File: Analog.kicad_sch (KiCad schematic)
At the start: 17 parts, among them J6 Conn_01x04, U6 MCP602

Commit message: updated pics
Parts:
- C28, C33: value 100n -> 1n
- R11, R12: value 33R -> 160R
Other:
- note added: "LowPass Filt. Fg = 1MHz"
- note removed: "LowPass Filt. Fg = 48.2kHz"
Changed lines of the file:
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@@
-    (effects (font (size 1.27 1.27)) (justify left bottom))
-  )
-  (text "LowPass Filt. Fg = 48.2kHz" (at 167.64 82.55 90)
     (effects (font (size 1.27 1.27)) (justify left bottom))
   )
@@
     (effects (font (size 1.27 1.27)) (justify left bottom))
   )
-  (text "LowPass Filt. Fg = 48.2kHz" (at 52.07 80.01 90)
+  (text "LowPass Filt. Fg = 1MHz" (at 52.07 80.01 90)
     (effects (font (size 1.27 1.27)) (justify left bottom))
   )
@@
   )
   (text "DC filter" (at 213.36 107.95 90)
+    (effects (font (size 1.27 1.27)) (justify left bottom))
+  )
+  (text "LowPass Filt. Fg = 1MHz" (at 166.37 81.28 90)
     (effects (font (size 1.27 1.27)) (justify left bottom))
   )
@@
       (effects (font (size 1.27 1.27)))
     )
-    (property "Value" "33R" (at 165.1 90.17 90)
+    (property "Value" "160R" (at 165.1 90.17 90)
       (effects (font (size 1.27 1.27)))
     )
@@
       (effects (font (size 1.27 1.27)))
     )
-    (property "Value" "100n" (at 172.72 92.71 0)
+    (property "Value" "1n" (at 172.72 92.71 0)
       (effects (font (size 1.27 1.27)))
     )
@@
       (effects (font (size 1.27 1.27)))
     )
-    (property "Value" "100n" (at 58.42 90.17 0)
+    (property "Value" "1n" (at 58.42 90.17 0)
       (effects (font (size 1.27 1.27)))
     )
@@
       (effects (font (size 1.27 1.27)))
     )
-    (property "Value" "33R" (at 50.8 87.63 90)
-      (effects (font (size 1.27 1.27)))
-    )
+    (property "Value" "160R" (at 50.8 87.63 90)
+      (effects (font (size 1.27 1.27)))
+    )

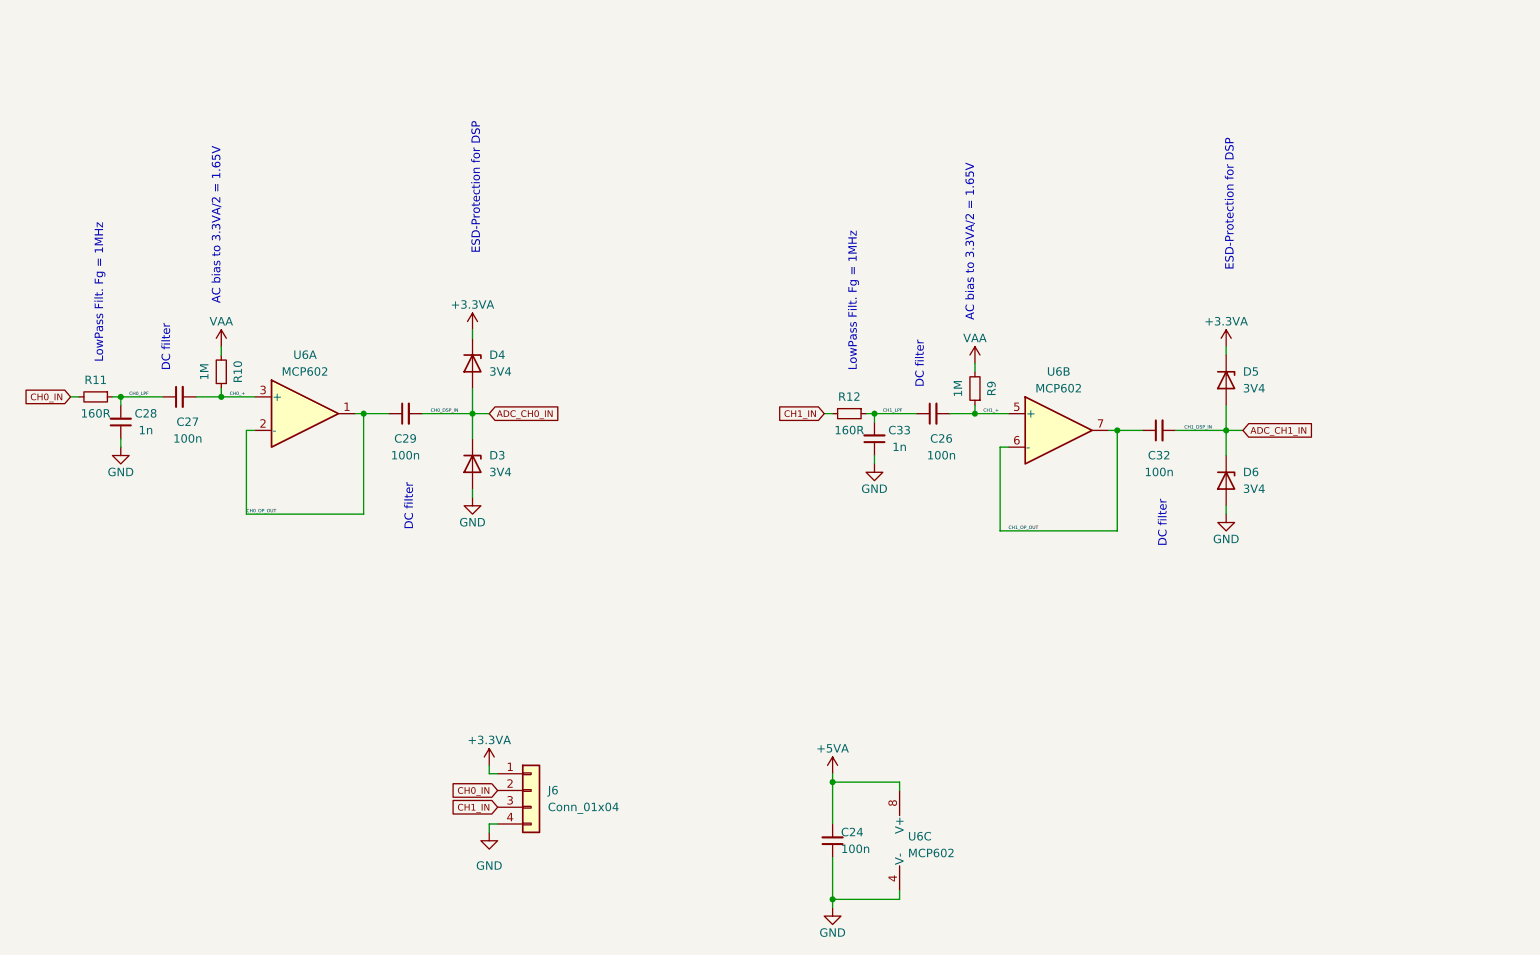
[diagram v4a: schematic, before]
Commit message: added DAC and an onboard fixed oscilltor to quickly test the DSP
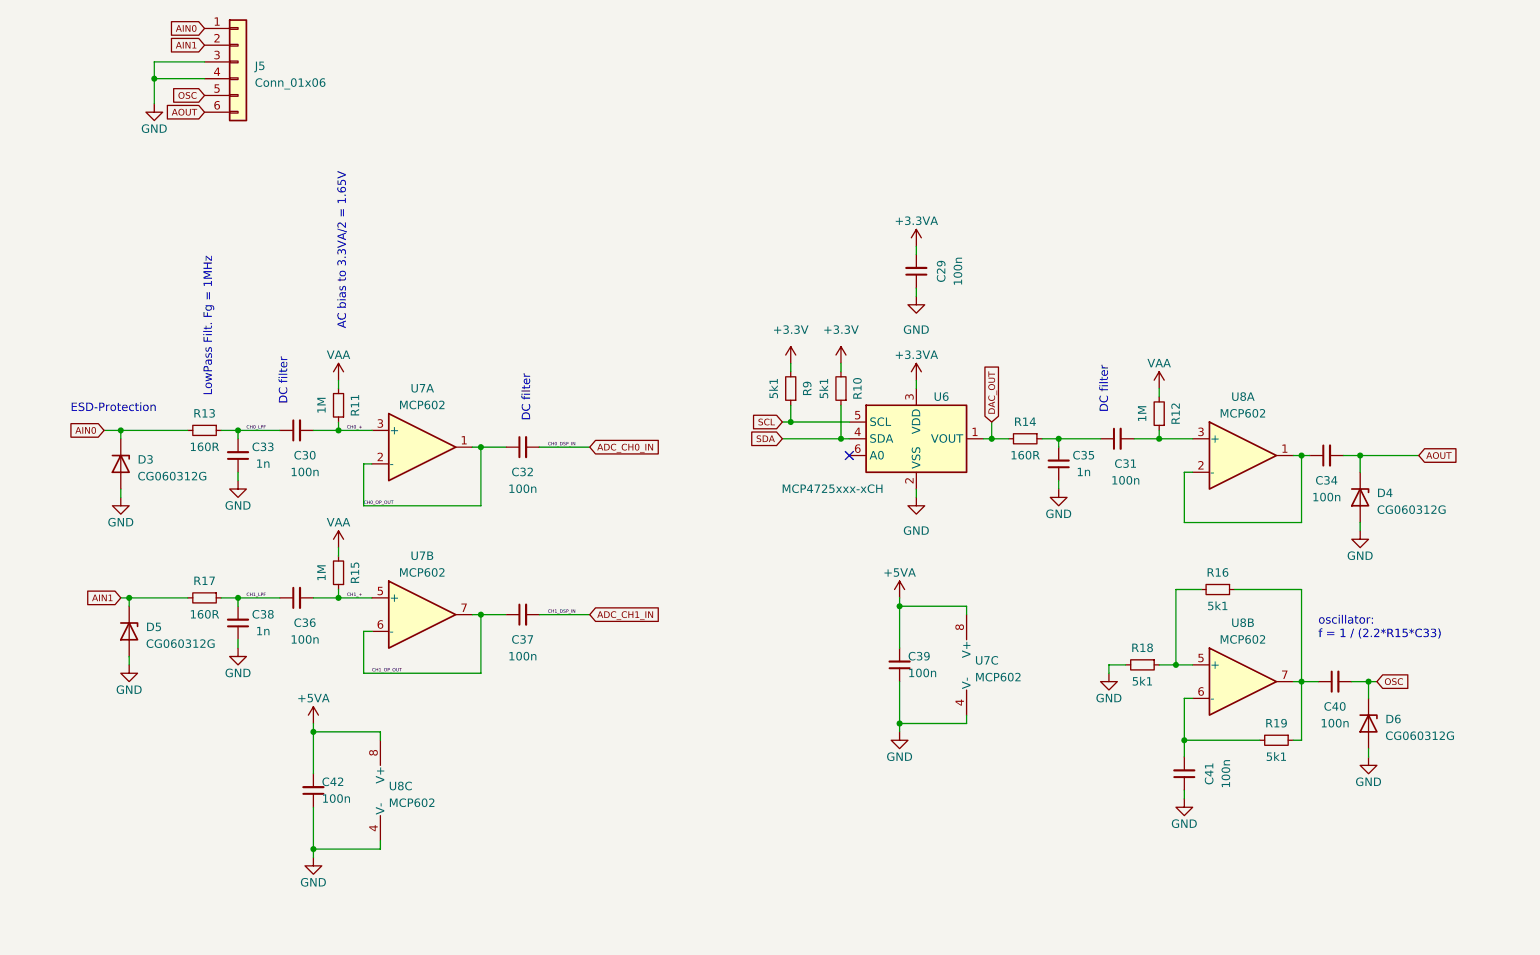
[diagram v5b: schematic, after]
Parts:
- removed D3, D4, D5, D6: 3V4, Diode_SMD:D_SOD-123F, symbol Device:D_Zener
- removed J6: Conn_01x04, Connector_PinHeader_2.54mm:PinHeader_1x04_P2.54mm_Vertical, symbol Connector_Generic:Conn_01x04
- added C29, C31, C34, C39, C40, C41: 100n, Capacitor_SMD:C_0603_1608Metric_Pad1.08x0.95mm_HandSolder, symbol Device:C_Small
- added C35: 1n, Capacitor_SMD:C_0603_1608Metric_Pad1.08x0.95mm_HandSolder, symbol Device:C_Small
- added D3, D4, D5, D6: CG060312G, Diode_SMD:D_0603_1608Metric_Pad1.05x0.95mm_HandSolder, symbol Diode:ESD5Zxx
- added J5: Conn_01x06, Connector_PinHeader_2.54mm:PinHeader_1x06_P2.54mm_Vertical, symbol Connector_Generic:Conn_01x06
- added R10, R16, R18, R19, R9: 5k1, Resistor_SMD:R_0603_1608Metric_Pad0.98x0.95mm_HandSolder, symbol Device:R_Small
- added R12: 1M, Resistor_SMD:R_0603_1608Metric_Pad0.98x0.95mm_HandSolder, symbol Device:R_Small
- added R14: 160R, Resistor_SMD:R_0603_1608Metric_Pad0.98x0.95mm_HandSolder, symbol Device:R_Small
- added U6: MCP4725xxx-xCH, Package_TO_SOT_SMD:SOT-23-6, symbol Analog_DAC:MCP4725xxx-xCH
- added unit 3 of U7
- added unit 1 of U8
- added unit 2 of U8
- renumbered C27 to C30, C29 to C32, C28 to C33, C26 to C36, C32 to C37, C33 to C38, C24 to C42, R10 to R11, R11 to R13, R9 to R15, R12 to R17, U6 to U7, U6 to U8
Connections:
- net +3.3VA: now also C29.2, U6.3 (VDD)
- net +5VA: now also C39.2, U7.8 (V+)
- net GND: now also C29.1, C35.1, C39.1, C41.1, D3.2 (A), D4.2 (A), D5.2 (A), D6.2 (A), J5.3 (Pin_3), J5.4 (Pin_4), R18.2, U6.2 (VSS), U7.4 (V-)
- net VAA: now also R12.2
- net CH0_IN renamed AIN0
- net AIN0: now also D3.1 (K), J5.1 (Pin_1)
- net CH1_IN renamed AIN1
- net AIN1: now also D5.1 (K), J5.2 (Pin_2)
- new net: C31.2, R12.1, U8.3 (+)
- new net: C31.1, C35.2, R14.1
- new net: C41.2, R19.2, U8.6 (-)
- new net: R16.2, R18.1, U8.5 (+)
- new net: C34.1, U8.1, U8.2 (-)
- new net: C40.1, R16.1, R19.1, U8.7
- new net +3V3: R10.2, R9.2
- new net AOUT: C34.2, D4.1 (K), J5.6 (Pin_6)
- new net DAC_OUT: R14.2, U6.1 (VOUT)
- new net OSC: C40.2, D6.1 (K), J5.5 (Pin_5)
- new net SCL: R9.1, U6.5 (SCL)
- new net SDA: R10.1, U6.4 (SDA)
- no-connect marks 0 -> 1
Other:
- note added: "ESD-Protection"
- note added: "oscillator: f = 1 / (2.2*R15*C33)"
- note removed: "ESD-Protection for DSP"
- moved on the sheet: C30, C32, C33, C36, C37, C38, C42, R11, R13, R15, R17, U7A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

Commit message: cleanup
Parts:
- added R20: 160R, Resistor_SMD:R_0603_1608Metric_Pad0.98x0.95mm_HandSolder, symbol Device:R_Small
- added R5: 5k1, Resistor_SMD:R_0603_1608Metric_Pad0.98x0.95mm_HandSolder, symbol Device:R_Small
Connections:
- net +5VA: now also R5.1
- net at R16.2, R18.1, U8.5 (+): now also R5.2
- net at R16.1, R19.1, U8.7: now also R20.2; no longer C40.1
- new net: C40.1, R20.1
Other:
- note added: "oscillator: f = 1 / (2.2*R19*C41) f+20% = 1 / (2.2*5151R*120nF) = 1125Hz fnom = 1 / (2.2*5100R*100nF) = 891Hz f-20% = 1 / (2.2*5049R*120nF) = 735Hz"
- note removed: "oscillator: f = 1 / (2.2*R15*C33)"
- moved on the sheet: C40, C41, D6, J5, R16, R18, R19, U8B

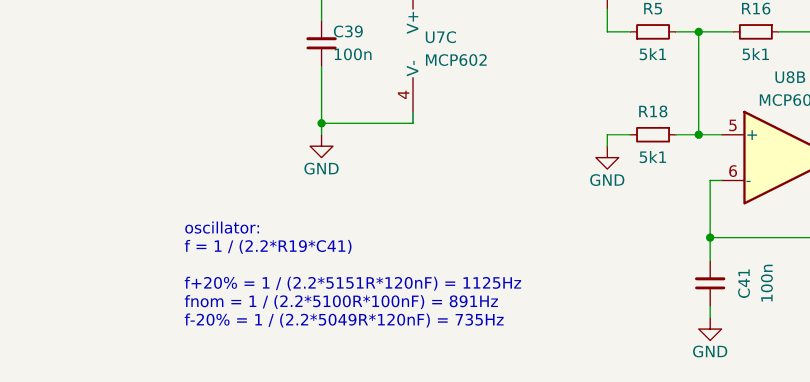
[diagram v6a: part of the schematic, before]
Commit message: implementing test ram function
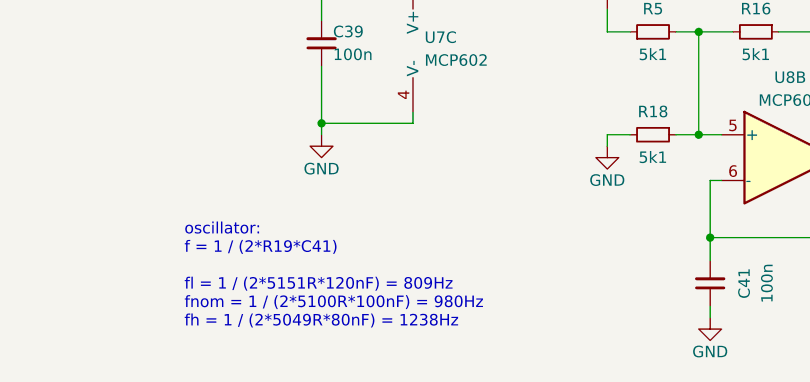
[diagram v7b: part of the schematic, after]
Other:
- note added: "oscillator: f = 1 / (2*R19*C41) fl = 1 / (2*5151R*120nF) = 809Hz fnom = 1 / (2*5100R*100nF) = 980Hz fh = 1 / (2*5049R*80nF) = 1238Hz"
- note removed: "oscillator: f = 1 / (2.2*R19*C41) f+20% = 1 / (2.2*5151R*120nF) = 1125Hz fnom = 1 / (2.2*5100R*100nF) = 891Hz f-20% = 1 / (2.2*5049R*120nF) = 735Hz"
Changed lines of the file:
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@@
     (effects (font (size 1.27 1.27)) (justify left bottom))
   )
-  (text "oscillator:\nf = 1 / (2.2*R19*C41)\n\nf+20% = 1 / (2.2*5151R*120nF) = 1125Hz\nfnom = 1 / (2.2*5100R*100nF) = 891Hz\nf-20% = 1 / (2.2*5049R*120nF) = 735Hz"
+  (text "oscillator:\nf = 1 / (2*R19*C41)\n\nfl = 1 / (2*5151R*120nF) = 809Hz\nfnom = 1 / (2*5100R*100nF) = 980Hz\nfh = 1 / (2*5049R*80nF) = 1238Hz"
     (at 157.48 157.48 0)
     (effects (font (size 1.27 1.27)) (justify left bottom))

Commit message: modifications for rev 3
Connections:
- net +3.3VA is gone; now on net +3V3: C29.2, U6.3 (VDD)
- net +5VA renamed +5V
